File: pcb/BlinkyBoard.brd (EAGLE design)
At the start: 26 x 10 mm, 23 parts, among them Q1 16 MHz

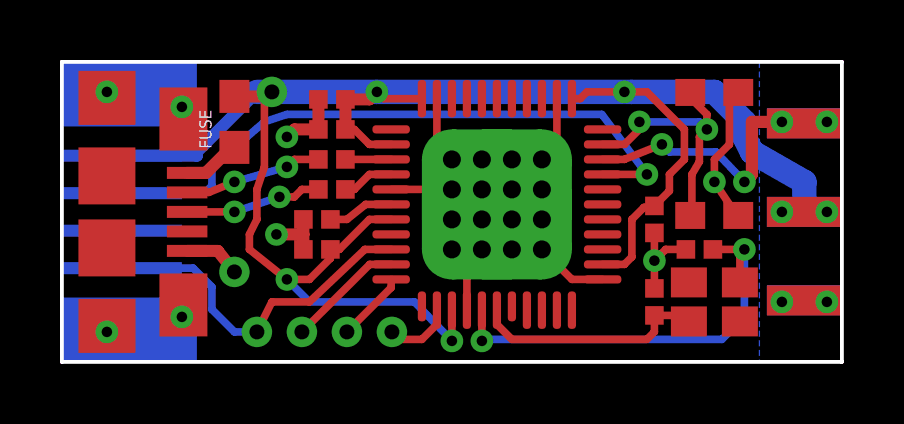
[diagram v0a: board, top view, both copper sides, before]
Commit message: Fuses are for suckers.
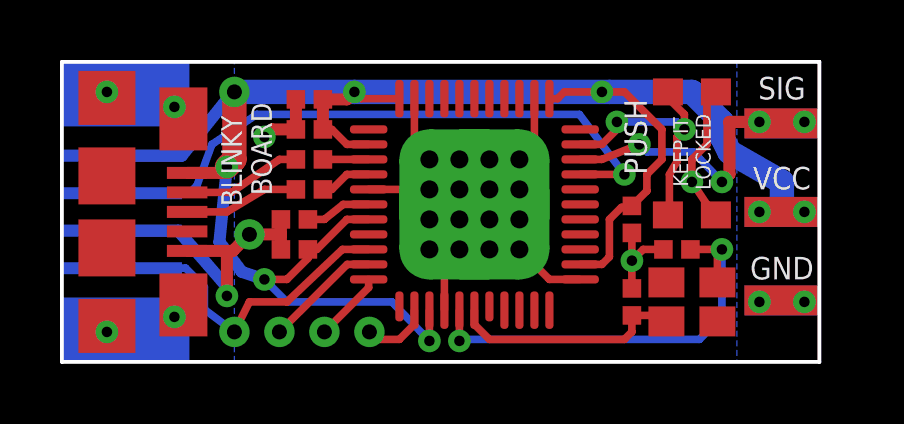
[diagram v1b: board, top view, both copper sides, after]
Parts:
- removed FUSE: PTC0603, SparkFun-PowerIC:0603
- moved U$7 1.35 mm to (6.25, 4.25)
- moved U$8 1.25 mm to (5.75, 9.00)
- moved C1 0.75 mm to (8.25, 8.75)
- moved C2 0.75 mm to (8.25, 7.75)
- moved C3 0.75 mm to (7.75, 3.75)
- moved C4 0.75 mm to (19.0, 4.75)
- moved C5 0.75 mm to (7.75, 4.75)
- moved C6 0.75 mm to (20.5, 3.75)
- moved C7 0.75 mm to (19.0, 2.00)
- moved Q1 0.75 mm to (21.0, 2.00)
- moved R1 0.75 mm to (8.25, 5.75)
- moved R2 0.75 mm to (8.25, 6.75)
- moved U$1 0.75 mm to (8.75, 1.00)
- moved U$2 0.75 mm to (13.8, 5.25)
- moved U$3 0.75 mm to (7.25, 1.00)
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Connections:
- removed net N$1: FUSE.1, U$4.P$1
- net VCC: now also U$4.P$1; no longer FUSE.2
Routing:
- net GND: track 27.4 -> 34.1 mm
- net N$1: track 2.07 -> 0.00 mm
- net SCK: track 11.6 -> 10.8 mm
- net D+_IN: track 4.56 -> 3.83 mm, vias 2 -> 0
- net ANALOG_IN: track 21.3 -> 20.6 mm
- net D-_IN: track 4.62 -> 3.97 mm, vias 2 -> 0
- net VCC: track 64.9 -> 64.5 mm, vias 6 -> 7
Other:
- board size 26 x 10 mm -> 25.2 x 10 mm
- board text added: "BLINKY"
- board text added: "BOARD"
- board text added: "GND"
- board text added: "KEEP IT LOCKED"
- board text added: "PUSH"
- board text added: "SIG"
- board text added: "VCC"

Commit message: Board is routed! Now just add silk
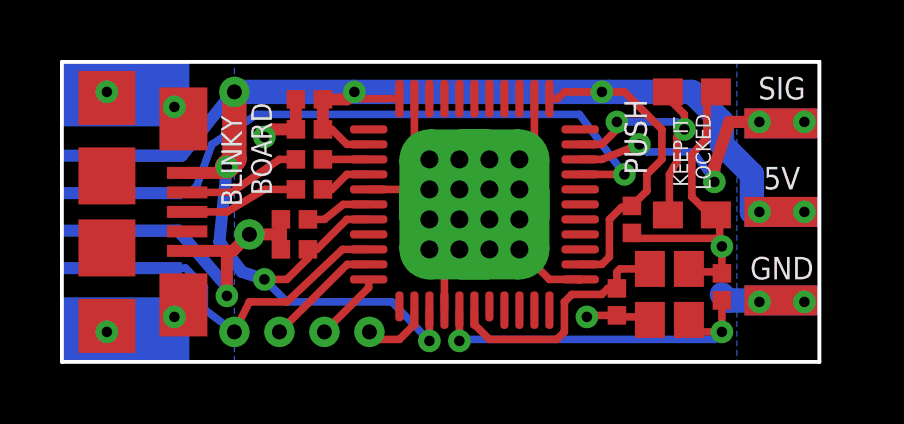
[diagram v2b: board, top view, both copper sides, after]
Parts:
- moved C6 1.95 mm to (22.0, 2.50), turned to 90 degrees
- moved Q1 0.79 mm to (20.2, 2.25), turned to 270 degrees
- moved C7 0.50 mm to (18.5, 2.00), turned to 270 degrees
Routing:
- net GND: track 34.1 -> 39.9 mm
- net N$8: track 14.6 -> 12.3 mm
- net N$1: track 0.00 -> 1.00 mm
- net N$9: track 7.90 -> 8.41 mm
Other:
- board text added: "5V"
- board text removed: "VCC"

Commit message: Silks added, routing cleaned up on bottom. Ready for release?
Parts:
- added U$9: (no value), blinkiverse:OSHW-LOGO-M
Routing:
- net VCC: track 64.8 -> 65.3 mm
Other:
- board text added: "Blinky board"
- board text added: "blinkiverse.com/bb"
- board text removed: "Blinkyboard"

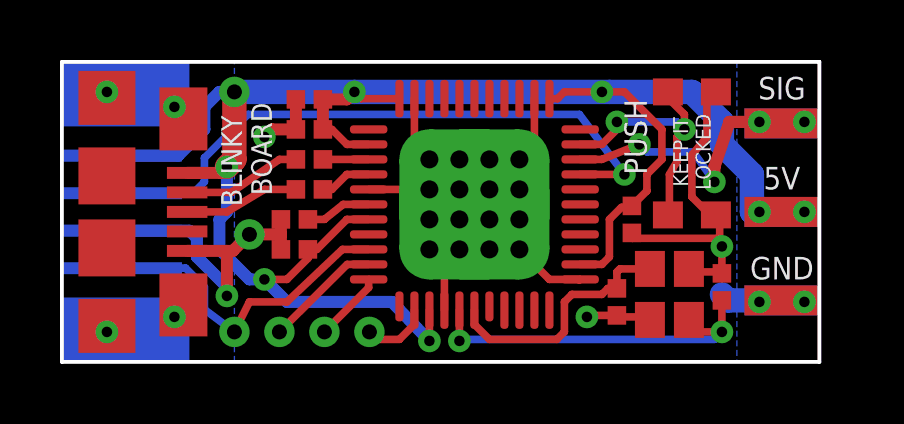
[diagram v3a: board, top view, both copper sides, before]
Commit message: PCB: replace smt USB connector with thru-hole version
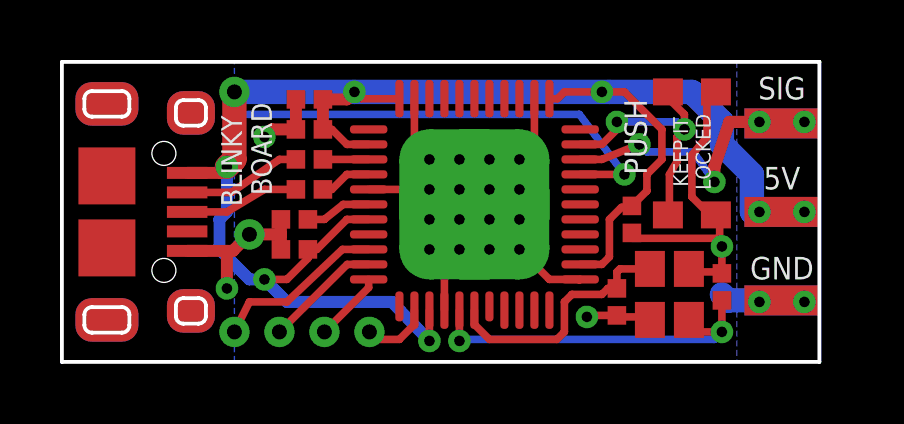
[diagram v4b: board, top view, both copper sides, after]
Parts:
- removed JP1: (no value), blinkiverse:SMT_PAD-5.5MM-4
- U$4: value MICRO_USB -> MICRO_USBSMT+DIP; device blinkiverse:MICRO_USB_FCI -> blinkiverse:MICRO_USB_THRUHOLE
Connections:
- net ANALOG_IN: no longer JP1.P$2
- net GND: no longer JP1.P$3
- net SCK: no longer JP1.P$4
- net VCC: no longer JP1.P$1
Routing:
- net ANALOG_IN: track 20.8 -> 15.0 mm
- net GND: track 40.2 -> 35.0 mm
- net VCC: track 65.3 -> 60.3 mm
- net SCK: track 10.8 -> 5.79 mm
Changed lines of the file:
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@@
 <grid distance="0.25" unitdist="mm" unit="mm" style="lines" multiple="1" display="no" altdistance="0.1" altunitdist="mm" altunit="mm"/>
 <layers>
-<layer number="1" name="Top" color="4" fill="1" visible="no" active="yes"/>
+<layer number="1" name="Top" color="4" fill="1" visible="yes" active="yes"/>
 <layer number="2" name="Route2" color="1" fill="3" visible="no" active="no"/>
 <layer number="3" name="Route3" color="4" fill="3" visible="no" active="no"/>
@@
 <layer number="19" name="Unrouted" color="6" fill="1" visible="yes" active="yes"/>
 <layer number="20" name="Dimension" color="15" fill="1" visible="yes" active="yes"/>
-<layer number="21" name="tPlace" color="11" fill="1" visible="no" active="yes"/>
-<layer number="22" name="bPlace" color="3" fill="1" visible="no" active="yes"/>
-<layer number="23" name="tOrigins" color="7" fill="1" visible="no" active="yes"/>
+<layer number="21" name="tPlace" color="11" fill="1" visible="yes" active="yes"/>
+<layer number="22" name="bPlace" color="3" fill="1" visible="yes" active="yes"/>
+<layer number="23" name="tOrigins" color="7" fill="1" visible="yes" active="yes"/>
 <layer number="24" name="bOrigins" color="7" fill="1" visible="yes" active="yes"/>
 <layer number="25" name="tNames" color="7" fill="1" visible="no" active="yes"/>
-<layer number="26" name="bNames" color="7" fill="1" visible="yes" active="yes"/>
+<layer number="26" name="bNames" color="7" fill="1" visible="no" active="yes"/>
 <layer number="27" name="tValues" color="7" fill="1" visible="no" active="yes"/>
 <layer number="28" name="bValues" color="7" fill="1" visible="no" active="yes"/>
@@
 <layer number="44" name="Drills" color="7" fill="1" visible="no" active="yes"/>
 <layer number="45" name="Holes" color="7" fill="1" visible="no" active="yes"/>
-<layer number="46" name="Milling" color="3" fill="1" visible="no" active="yes"/>
+<layer number="46" name="Milling" color="3" fill="1" visible="yes" active="yes"/>
 <layer number="47" name="Measures" color="7" fill="1" visible="no" active="yes"/>
 <layer number="48" name="Document" color="7" fill="1" visible="no" active="yes"/>
@@
  board</text>
 <text x="8.75" y="3.75" size="0.8128" layer="26" font="vector" ratio="20" rot="MR0" align="center">Rev B</text>
-<rectangle x1="0" y1="7.85" x2="4.25" y2="10" layer="16"/>
-<rectangle x1="0" y1="0" x2="4.25" y2="2.15" layer="16"/>
 <text x="24" y="8.75" size="0.75" layer="25" font="vector" ratio="15" align="bottom-center">SIG</text>
 <text x="24" y="5.75" size="0.75" layer="25" font="vector" ratio="15" align="bottom-center">5V</text>
@@
 <element name="C4" library="blinkiverse" package="CAP_0402_KEMET_MEDIAN" value="0.1uF" x="19" y="4.75" smashed="yes" rot="R270"/>
 <element name="WS1" library="blinkiverse" package="WS2811_CONNECTOR" value="WS2811_CONNECTOR" x="24" y="5"/>
-<element name="U$4" library="blinkiverse" package="MICRO_USB_FCI" value="MICRO_USB" x="1.5" y="5" rot="R270"/>
+<element name="U$4" library="blinkiverse" package="MICRO_USB_THRUHOLE" value="MICRO_USBSMT+DIP" x="1.5" y="5" rot="R270"/>
 <element name="U$1" library="blinkiverse" package="TEST_VIA_.5MM" value="TEST_VIA" x="8.75" y="1"/>
 <element name="U$3" library="blinkiverse" package="TEST_VIA_.5MM" value="TEST_VIA" x="7.25" y="1"/>
@@
 <element name="U$8" library="blinkiverse" package="TEST_VIA_.5MM" value="TEST_VIA" x="5.75" y="9"/>
 <element name="WS3" library="blinkiverse" package="WS2811_CONNECTOR" value="WS2811_CONNECTOR" x="24" y="5" rot="MR0"/>
-<element name="JP1" library="blinkiverse" package="SMT_PAD-5.5MM-4" value="" x="2" y="5" rot="MR270"/>
 <element name="U$9" library="blinkiverse" package="OSHW-LOGO-M" value="" x="19" y="5" rot="MR0"/>
 </elements>
@@
 <wire x1="5.7" y1="3.7" x2="6.25" y2="4.25" width="0.4" layer="1"/>
 <wire x1="6.25" y1="4.25" x2="7.3" y2="4.25" width="0.4" layer="1"/>
-<via x="5.5" y="2.2" extent="1-16" drill="0.35"/>
-<wire x1="5.5" y1="2.2" x2="5.5" y2="3.7" width="0.4" layer="1"/>
-<contactref element="JP1" pad="P$3"/>
+<via x="5.5" y="2.45" extent="1-16" drill="0.35"/>
+<wire x1="5.5" y1="2.45" x2="5.5" y2="3.7" width="0.4" layer="1"/>
 <wire x1="19" y1="4.3" x2="18.95" y2="4.3" width="0.254" layer="1"/>
 <wire x1="18.95" y1="4.3" x2="19" y2="4.12" width="0.254" layer="1"/>
@@
 <wire x1="22.2" y1="2.05" x2="22" y2="2.25" width="0.8128" layer="16"/>
 <wire x1="22" y1="3" x2="21" y2="3" width="0.254" layer="1"/>
-<wire x1="2" y1="4.375" x2="4.25" y2="4.375" width="0.4" layer="16"/>
-<wire x1="4.25" y1="4.375" x2="4.5" y2="4.125" width="0.4" layer="16"/>
-<wire x1="4.5" y1="4.125" x2="4.5" y2="3.5" width="0.4" layer="16"/>
-<wire x1="4.5" y1="3.5" x2="5.5" y2="2.5" width="0.4" layer="16"/>
-<wire x1="5.5" y1="2.5" x2="5.5" y2="2.2" width="0.4" layer="16"/>
 </signal>
 <signal name="MOSI">
@@
 <wire x1="7.5" y1="2" x2="6.25" y2="2" width="0.254" layer="1"/>
 <wire x1="6.25" y1="2" x2="5.75" y2="1" width="0.254" layer="1"/>
-<contactref element="JP1" pad="P$4"/>
-<wire x1="2" y1="3.125" x2="4.125" y2="3.125" width="0.254" layer="16"/>
-<wire x1="4.125" y1="3.125" x2="4.75" y2="2.5" width="0.254" layer="16"/>
-<wire x1="4.75" y1="2.5" x2="4.75" y2="1.75" width="0.254" layer="16"/>
-<wire x1="4.75" y1="1.75" x2="5.75" y2="1" width="0.254" layer="16"/>
 </signal>
 <signal name="RST">
@@
 <wire x1="18.75" y1="6.25" x2="17.25" y2="8.25" width="0.254" layer="16"/>
 <wire x1="17.25" y1="8.25" x2="6.2" y2="8.25" width="0.254" layer="16"/>
-<contactref element="JP1" pad="P$2"/>
-<wire x1="2" y1="5.625" x2="4.375" y2="5.625" width="0.254" layer="16"/>
-<wire x1="4.375" y1="5.625" x2="4.75" y2="6" width="0.254" layer="16"/>
-<wire x1="4.75" y1="6" x2="4.75" y2="6.8" width="0.254" layer="16"/>
-<wire x1="4.75" y1="6.8" x2="6.2" y2="8.25" width="0.254" layer="16"/>
 </signal>
 <signal name="LED_DATA">
@@
 </signal>
 <signal name="VCC">
-<contactref element="JP1" pad="P$1"/>
 <contactref element="C1" pad="P$1"/>
 <contactref element="U$2" pad="34"/>
@@
 <wire x1="4.175" y1="6.3" x2="5.3" y2="6.3" width="0.4" layer="1"/>
 <wire x1="5.3" y1="6.3" x2="5.5" y2="6.5" width="0.4" layer="1"/>
-<wire x1="2" y1="6.875" x2="3.875" y2="6.875" width="0.4" layer="16"/>
-<wire x1="5.75" y1="9" x2="5.25" y2="9" width="0.4" layer="16"/>
-<wire x1="5.25" y1="9" x2="4.75" y2="8.5" width="0.4" layer="16"/>
-<wire x1="4.75" y1="8.5" x2="4.75" y2="7.75" width="0.4" layer="16"/>
-<wire x1="4.75" y1="7.75" x2="3.875" y2="6.875" width="0.4" layer="16"/>
 </signal>
 <signal name="N$3">
-<via x="1.5" y="9" extent="1-16" drill="0.35"/>
 </signal>
 <signal name="N$4">
-<via x="1.5" y="1" extent="1-16" drill="0.35"/>
 </signal>
 <signal name="N$5">
-<via x="3.75" y="8.5" extent="1-16" drill="0.35"/>
 </signal>
 <signal name="N$6">
-<via x="3.75" y="1.5" extent="1-16" drill="0.35"/>
 </signal>
 <signal name="N$1">

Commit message: Switch to thru-hole micro usb, add expansion pads on the bottom, make thermal vias on the processor smaller.
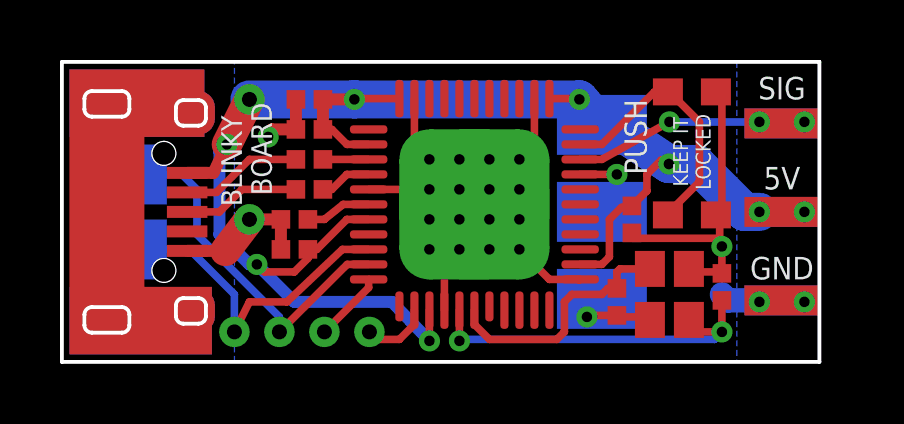
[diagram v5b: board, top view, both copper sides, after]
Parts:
- removed U$9: (no value), blinkiverse:OSHW-LOGO-M
- added U$10, U$11, U$12, U$13, U$14: TEST_PAD_SMT, blinkiverse:TEST_PAD_SMT
- added U$15: (no value), blinkiverse:OSHW-LOGO-S
- moved U$8 0.56 mm to (6.25, 8.75)
- moved U$7 0.50 mm to (6.25, 4.75)
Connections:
- net ANALOG_IN: now also U$11.P$1
- net GND: now also U$13.P$1
- net MOSI: now also U$14.P$1
- net SCK: now also U$10.P$1
- net VCC: now also U$12.P$1
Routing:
- net ANALOG_IN: track 15.0 -> 2.68 mm
- net MOSI: track 3.90 -> 12.5 mm
- net VCC: track 60.3 -> 54.2 mm, vias 7 -> 8
- net SCK: track 5.79 -> 11.4 mm
- net LED_DATA: track 10.7 -> 8.68 mm, vias 4 -> 3
- net GND: track 35.0 -> 33.4 mm, vias 6 -> 5
- net N$10: track 9.70 -> 8.92 mm, vias 2 -> 0
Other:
- board text added: "Blinky Tape"
- board text added: "Rev C"
- board text added: "blinkytape.com"
- board text removed: "Blinky board"
- board text removed: "Rev B"
- board text removed: "blinkiverse.com/bb"
